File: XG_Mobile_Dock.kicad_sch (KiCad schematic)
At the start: 22 parts, among them J1 5-1775443-8, J12 USB_C_Receptacle, J17 8730, J2 20455-040E-76, J3 20455-040E-76, J4 3-2362375-4, J7 Conn_02x10_Odd_Even, J8 Conn_02x10_Odd_Even

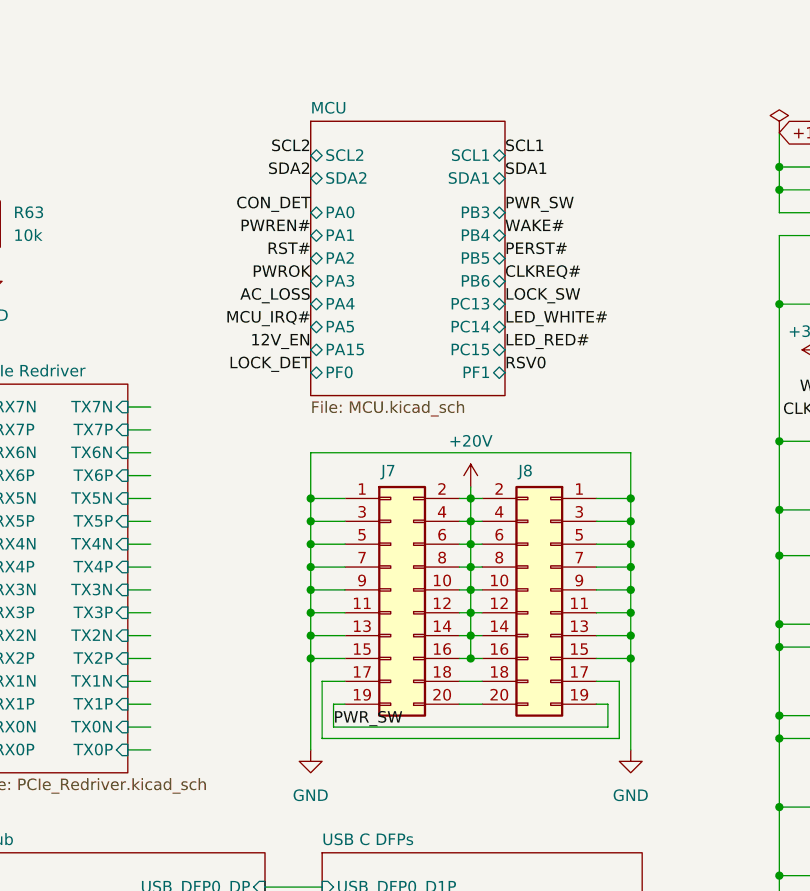
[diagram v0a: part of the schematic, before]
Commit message: Improvements to board
* Break up power switch into input and output signals
* Removed POWER_EN from USB PD charger (GPIO does not work due to one event per pin)
* Added MOSFET to buffer GPIO output from PD IC
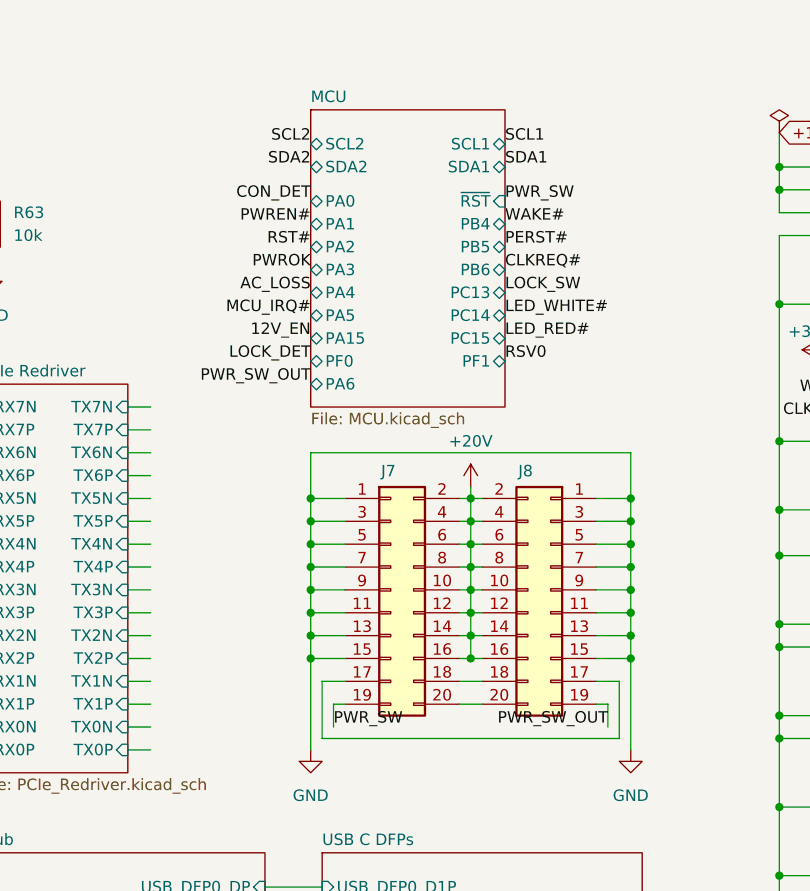
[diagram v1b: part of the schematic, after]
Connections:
- net PWR_SW: no longer J8.19 (Pin_19)
- new net PWR_SW_OUT: J8.19 (Pin_19)
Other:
- sheet MCU ports: added PA6, ~{RST}; removed PB3
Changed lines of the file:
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@@
 	(wire
 		(pts
-			(xy 139.7 90.17) (xy 170.18 90.17)
-		)
-		(stroke
-			(width 0)
-			(type default)
-		)
-	)
-	(wire
-		(pts
 			(xy 231.14 71.12) (xy 231.14 73.66)
 		)
@@
 	)
 	(label "PWROK"
-		(at 137.16 40.64 180)
+		(at 137.16 39.37 180)
 		(fields_autoplaced yes)
 		(effects
@@
 	)
 	(label "RSV0"
-		(at 158.75 50.8 0)
+		(at 158.75 49.53 0)
 		(fields_autoplaced yes)
 		(effects
@@
 	)
 	(label "SDA1"
-		(at 158.75 29.21 0)
+		(at 158.75 27.94 0)
 		(fields_autoplaced yes)
 		(effects
@@
 	)
 	(label "SDA2"
-		(at 137.16 29.21 180)
+		(at 137.16 27.94 180)
 		(fields_autoplaced yes)
 		(effects
@@
 	)
 	(label "SCL1"
-		(at 158.75 26.67 0)
+		(at 158.75 25.4 0)
 		(fields_autoplaced yes)
 		(effects
@@
 	)
 	(label "SCL2"
-		(at 137.16 26.67 180)
+		(at 137.16 25.4 180)
 		(fields_autoplaced yes)
 		(effects
@@
 	)
 	(label "CON_DET"
-		(at 137.16 33.02 180)
+		(at 137.16 31.75 180)
 		(fields_autoplaced yes)
 		(effects
@@
 	)
 	(label "12V_EN"
-		(at 137.16 48.26 180)
+		(at 137.16 46.99 180)
 		(fields_autoplaced yes)
 		(effects
@@
 	)
 	(label "CLKREQ#"
-		(at 158.75 40.64 0)
+		(at 158.75 39.37 0)
 		(fields_autoplaced yes)
 		(effects
@@
 	)
 	(label "PWREN#"
-		(at 137.16 35.56 180)
+		(at 137.16 34.29 180)
 		(fields_autoplaced yes)
 		(effects
@@
 	)
 	(label "LED_RED#"
-		(at 158.75 48.26 0)
+		(at 158.75 46.99 0)
 		(fields_autoplaced yes)
 		(effects
@@
 	)
 	(label "LOCK_SW"
-		(at 158.75 43.18 0)
+		(at 158.75 41.91 0)
 		(fields_autoplaced yes)
 		(effects
@@
 	)
 	(label "PERST#"
-		(at 158.75 38.1 0)
+		(at 158.75 36.83 0)
 		(fields_autoplaced yes)
 		(effects
@@
 	)
 	(label "LED_WHITE#"
-		(at 158.75 45.72 0)
+		(at 158.75 44.45 0)
 		(fields_autoplaced yes)
 		(effects
@@
 	)
 	(label "AC_LOSS"
-		(at 137.16 43.18 180)
+		(at 137.16 41.91 180)
 		(fields_autoplaced yes)
 		(effects
@@
 	)
 	(label "MCU_IRQ#"
-		(at 137.16 45.72 180)
+		(at 137.16 44.45 180)
 		(fields_autoplaced yes)
 		(effects
@@
 	)
 	(label "WAKE#"
-		(at 158.75 35.56 0)
+		(at 158.75 34.29 0)
 		(fields_autoplaced yes)
 		(effects
@@
 	)
 	(label "RST#"
-		(at 137.16 38.1 180)
+		(at 137.16 36.83 180)
 		(fields_autoplaced yes)
 		(effects
@@
 	)
 	(label "PWR_SW"
-		(at 158.75 33.02 0)
+		(at 158.75 31.75 0)
 		(fields_autoplaced yes)
 		(effects
@@
 		)
 	)
+	(label "PWR_SW_OUT"
+		(at 170.18 90.17 180)
+		(fields_autoplaced yes)
+		(effects
+			(font
+				(size 1.27 1.27)
+			)
+			(justify right bottom)
+		)
+	)
 	(label "C_RXN"
 		(at 40.64 85.09 0)
@@
 	)
 	(label "LOCK_DET"
-		(at 137.16 50.8 180)
+		(at 137.16 49.53 180)
 		(fields_autoplaced yes)
 		(effects
@@
 		)
 	)
+	(label "PWR_SW_OUT"
+		(at 137.16 52.07 180)
+		(fields_autoplaced yes)
+		(effects
+			(font
+				(size 1.27 1.27)
+			)
+			(justify right bottom)
+		)
+	)
 	(label "RX3P"
 		(at 223.52 101.6 0)
@@
 	)
 	(sheet
-		(at 137.16 22.86)
-		(size 21.59 30.48)
+		(at 137.16 21.59)
+		(size 21.59 33.02)
 		(fields_autoplaced yes)
 		(stroke
@@
 		)
 		(property "Sheetname" "MCU"
-			(at 137.16 22.1484 0)
+			(at 137.16 20.8784 0)
 			(effects
 				(font
@@
 		)
 		(property "Sheetfile" "MCU.kicad_sch"
-			(at 137.16 53.9246 0)
+			(at 137.16 55.1946 0)
 			(effects
 				(font
@@
 		)
 		(pin "PA0" bidirectional
-			(at 137.16 33.02 180)
+			(at 137.16 31.75 180)
 			(effects
 				(font
@@
 		)
 		(pin "PA1" bidirectional
-			(at 137.16 35.56 180)
+			(at 137.16 34.29 180)
 			(effects
 				(font
@@
 		)
 		(pin "PA2" bidirectional
-			(at 137.16 38.1 180)
+			(at 137.16 36.83 180)
 			(effects
 				(font
@@
 		)
 		(pin "PA3" bidirectional
-			(at 137.16 40.64 180)
+			(at 137.16 39.37 180)
 			(effects
 				(font
@@
 		)
 		(pin "PA4" bidirectional
-			(at 137.16 43.18 180)
+			(at 137.16 41.91 180)
 			(effects
 				(font
@@
 		)
 		(pin "PA5" bidirectional
-			(at 137.16 45.72 180)
+			(at 137.16 44.45 180)
 			(effects
 				(font
@@
 		)
 		(pin "PA15" bidirectional
-			(at 137.16 48.26 180)
+			(at 137.16 46.99 180)
 			(effects
 				(font
@@
 		)
 		(pin "SDA2" bidirectional
-			(at 137.16 29.21 180)
+			(at 137.16 27.94 180)
 			(effects
 				(font
@@
 		)
 		(pin "SCL2" bidirectional
-			(at 137.16 26.67 180)
+			(at 137.16 25.4 180)
 			(effects
 				(font
@@
 		)
 		(pin "SCL1" bidirectional
-			(at 158.75 26.67 0)
+			(at 158.75 25.4 0)
 			(effects
 				(font
@@
 		)
 		(pin "SDA1" bidirectional
-			(at 158.75 29.21 0)
-			(effects
-				(font
-					(size 1.27 1.27)
-				)
-				(justify right)
-			)
-		)
-		(pin "PB3" bidirectional
-			(at 158.75 33.02 0)
+			(at 158.75 27.94 0)
 			(effects
 				(font
@@
 		)
 		(pin "PB4" bidirectional
-			(at 158.75 35.56 0)
+			(at 158.75 34.29 0)
 			(effects
 				(font
@@
 		)
 		(pin "PB5" bidirectional
-			(at 158.75 38.1 0)
+			(at 158.75 36.83 0)
 			(effects
 				(font
@@
 		)
 		(pin "PB6" bidirectional
-			(at 158.75 40.64 0)
+			(at 158.75 39.37 0)
 			(effects
 				(font
@@
 		)
 		(pin "PC13" bidirectional
-			(at 158.75 43.18 0)
+			(at 158.75 41.91 0)
 			(effects
 				(font
@@
 		)
 		(pin "PC14" bidirectional
-			(at 158.75 45.72 0)
+			(at 158.75 44.45 0)
 			(effects
 				(font
@@
 		)
 		(pin "PC15" bidirectional
-			(at 158.75 48.26 0)
+			(at 158.75 46.99 0)
 			(effects
 				(font
@@
 		)
 		(pin "PF0" bidirectional
-			(at 137.16 50.8 180)
+			(at 137.16 49.53 180)
 			(effects
 				(font
@@
 		)
 		(pin "PF1" bidirectional
-			(at 158.75 50.8 0)
+			(at 158.75 49.53 0)
+			(effects
+				(font
+					(size 1.27 1.27)
+				)
+				(justify right)
+			)
+		)
+		(pin "PA6" bidirectional
+			(at 137.16 52.07 180)
+			(effects
+				(font
+					(size 1.27 1.27)
+				)
+				(justify left)
+			)
+		)
+		(pin "~{RST}" input
+			(at 158.75 31.75 0)
 			(effects
 				(font

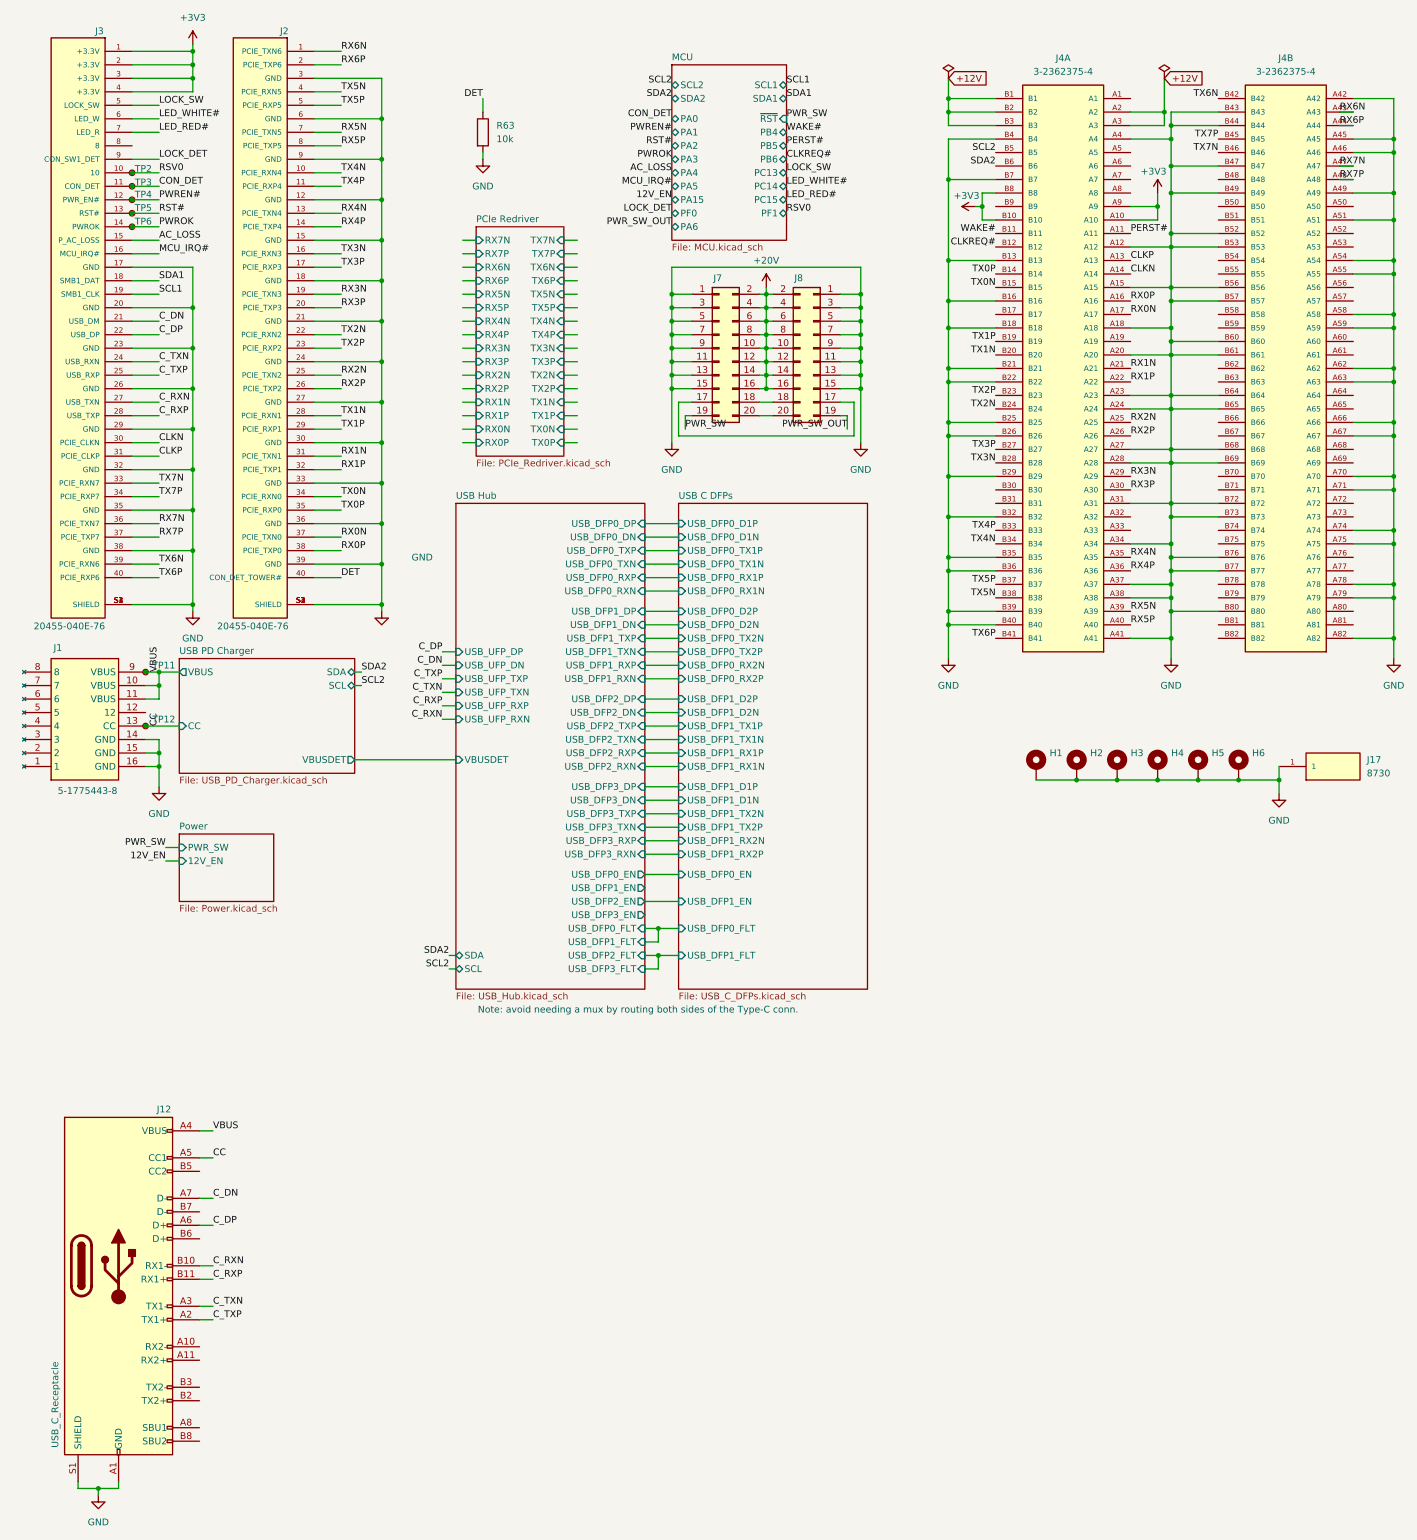
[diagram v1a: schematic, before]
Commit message: Fixed power connector, PCIe direction, and MCU changes
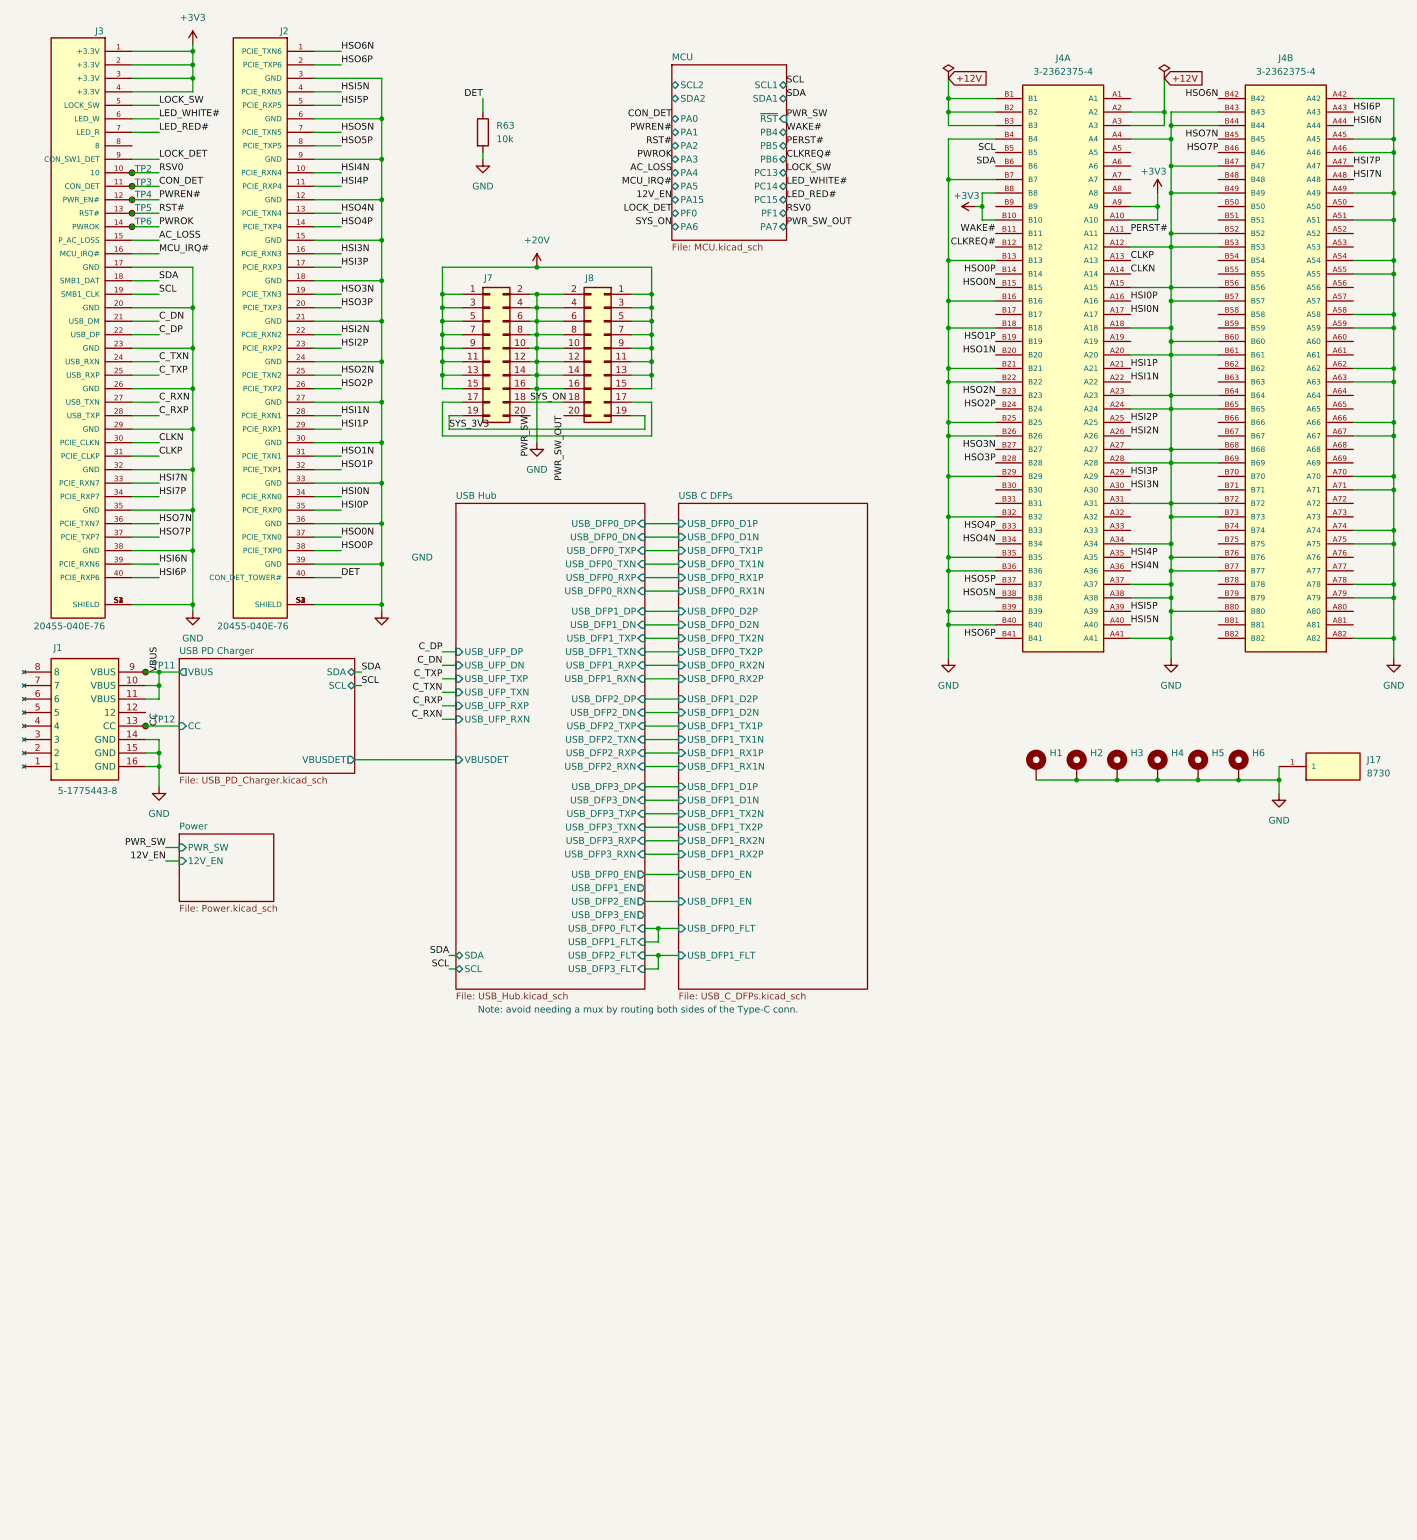
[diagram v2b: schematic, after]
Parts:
- removed J12: USB_C_Receptacle, USB-C-SMD_TYPE-C-24P-QT:USB-C-SMD_TYPE-C-24P-QT, symbol Connector:USB_C_Receptacle
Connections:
- net SCL2 is gone; now on net SCL: J4.B5
- net SDA2 is gone; now on net SDA: J4.B6
- net +20V: now also J7.1 (Pin_1), J7.11 (Pin_11), J7.13 (Pin_13), J7.15 (Pin_15), J7.3 (Pin_3), J7.5 (Pin_5), J7.7 (Pin_7), J7.9 (Pin_9), J8.1 (Pin_1), J8.11 (Pin_11), J8.13 (Pin_13), J8.15 (Pin_15), J8.3 (Pin_3), J8.5 (Pin_5), J8.7 (Pin_7), J8.9 (Pin_9); no longer J7.10 (Pin_10), J7.12 (Pin_12), J7.14 (Pin_14), J7.16 (Pin_16), J7.2 (Pin_2), J7.4 (Pin_4), J7.6 (Pin_6), J7.8 (Pin_8), J8.10 (Pin_10), J8.12 (Pin_12), J8.14 (Pin_14), J8.16 (Pin_16), J8.2 (Pin_2), J8.4 (Pin_4), J8.6 (Pin_6), J8.8 (Pin_8)
- net GND: now also J7.10 (Pin_10), J7.12 (Pin_12), J7.14 (Pin_14), J7.16 (Pin_16), J7.2 (Pin_2), J7.4 (Pin_4), J7.6 (Pin_6), J7.8 (Pin_8), J8.10 (Pin_10), J8.12 (Pin_12), J8.14 (Pin_14), J8.16 (Pin_16), J8.2 (Pin_2), J8.4 (Pin_4), J8.6 (Pin_6), J8.8 (Pin_8); no longer J7.1 (Pin_1), J7.11 (Pin_11), J7.13 (Pin_13), J7.15 (Pin_15), J7.3 (Pin_3), J7.5 (Pin_5), J7.7 (Pin_7), J7.9 (Pin_9), J8.1 (Pin_1), J8.11 (Pin_11), J8.13 (Pin_13), J8.15 (Pin_15), J8.3 (Pin_3), J8.5 (Pin_5), J8.7 (Pin_7), J8.9 (Pin_9)
- net PWR_SW: now also J7.20 (Pin_20); no longer J7.19 (Pin_19)
- net PWR_SW_OUT: now also J8.20 (Pin_20); no longer J8.19 (Pin_19)
- net SYS_ON: now reaches J7.18 (Pin_18), J8.18 (Pin_18)
- net RX0N renamed HSI0N
- net HSI0N: now also J2.34 (PCIE_RXN0); no longer J2.37 (PCIE_TXN0)
- net RX0P renamed HSI0P
- net HSI0P: now also J2.35 (PCIE_RXP0); no longer J2.38 (PCIE_TXP0)
- net RX1N renamed HSI1P
- net HSI1P: now also J2.29 (PCIE_RXP1); no longer J2.31 (PCIE_TXN1)
- net RX1P renamed HSI1N
- net HSI1N: now also J2.28 (PCIE_RXN1); no longer J2.32 (PCIE_TXP1)
- net RX2N renamed HSI2P
- net HSI2P: now also J2.23 (PCIE_RXP2); no longer J2.25 (PCIE_TXN2)
- net RX2P renamed HSI2N
- net HSI2N: now also J2.22 (PCIE_RXN2); no longer J2.26 (PCIE_TXP2)
- net RX3N renamed HSI3P
- net HSI3P: now also J2.17 (PCIE_RXP3); no longer J2.19 (PCIE_TXN3)
- net RX3P renamed HSI3N
- net HSI3N: now also J2.16 (PCIE_RXN3); no longer J2.20 (PCIE_TXP3)
- net RX4N renamed HSI4P
- net HSI4P: now also J2.11 (PCIE_RXP4); no longer J2.13 (PCIE_TXN4)
- net RX4P renamed HSI4N
- net HSI4N: now also J2.10 (PCIE_RXN4); no longer J2.14 (PCIE_TXP4)
- net RX5N renamed HSI5P
- net HSI5P: now also J2.5 (PCIE_RXP5); no longer J2.7 (PCIE_TXN5)
- net RX5P renamed HSI5N
- net HSI5N: now also J2.4 (PCIE_RXN5); no longer J2.8 (PCIE_TXP5)
- net RX6N renamed HSI6P
- net HSI6P: now also J3.40 (PCIE_RXP6); no longer J2.1 (PCIE_TXN6)
- net RX6P renamed HSI6N
- net HSI6N: now also J3.39 (PCIE_RXN6); no longer J2.2 (PCIE_TXP6)
- net RX7N renamed HSI7P
- net HSI7P: now also J3.34 (PCIE_RXP7); no longer J3.36 (PCIE_TXN7)
- net RX7P renamed HSI7N
- net HSI7N: now also J3.33 (PCIE_RXN7); no longer J3.37 (PCIE_TXP7)
- net SCL1 renamed SCL
- net SDA1 renamed SDA
- net TX0N renamed HSO0N
- net HSO0N: now also J2.37 (PCIE_TXN0); no longer J2.34 (PCIE_RXN0)
- net TX0P renamed HSO0P
- net HSO0P: now also J2.38 (PCIE_TXP0); no longer J2.35 (PCIE_RXP0)
- net TX1N renamed HSO1N
- net HSO1N: now also J2.31 (PCIE_TXN1); no longer J2.28 (PCIE_RXN1)
- net TX1P renamed HSO1P
- net HSO1P: now also J2.32 (PCIE_TXP1); no longer J2.29 (PCIE_RXP1)
- net TX2N renamed HSO2P
- net HSO2P: now also J2.26 (PCIE_TXP2); no longer J2.22 (PCIE_RXN2)
- net TX2P renamed HSO2N
- net HSO2N: now also J2.25 (PCIE_TXN2); no longer J2.23 (PCIE_RXP2)
- net TX3N renamed HSO3P
- net HSO3P: now also J2.20 (PCIE_TXP3); no longer J2.16 (PCIE_RXN3)
- net TX3P renamed HSO3N
- net HSO3N: now also J2.19 (PCIE_TXN3); no longer J2.17 (PCIE_RXP3)
- net TX4N renamed HSO4N
- net HSO4N: now also J2.13 (PCIE_TXN4); no longer J2.10 (PCIE_RXN4)
- net TX4P renamed HSO4P
- net HSO4P: now also J2.14 (PCIE_TXP4); no longer J2.11 (PCIE_RXP4)
- net TX5N renamed HSO5N
- net HSO5N: now also J2.7 (PCIE_TXN5); no longer J2.4 (PCIE_RXN5)
- net TX5P renamed HSO5P
- net HSO5P: now also J2.8 (PCIE_TXP5); no longer J2.5 (PCIE_RXP5)
- net TX6N renamed HSO6N
- net HSO6N: now also J2.1 (PCIE_TXN6); no longer J3.39 (PCIE_RXN6)
- net TX6P renamed HSO6P
- net HSO6P: now also J2.2 (PCIE_TXP6); no longer J3.40 (PCIE_RXP6)
- net TX7N renamed HSO7P
- net HSO7P: now also J3.37 (PCIE_TXP7); no longer J3.33 (PCIE_RXN7)
- net TX7P renamed HSO7N
- net HSO7N: now also J3.36 (PCIE_TXN7); no longer J3.34 (PCIE_RXP7)
- new net SYS_3V3: J7.19 (Pin_19), J8.19 (Pin_19)
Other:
- removed sheet PCIe Redriver
- sheet MCU ports: added PA7; removed none
- moved on the sheet: J7, J8
